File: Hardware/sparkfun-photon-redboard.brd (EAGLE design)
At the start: 68.6 x 53.3 mm, 54 parts, among them U1 WM-N-BM-14

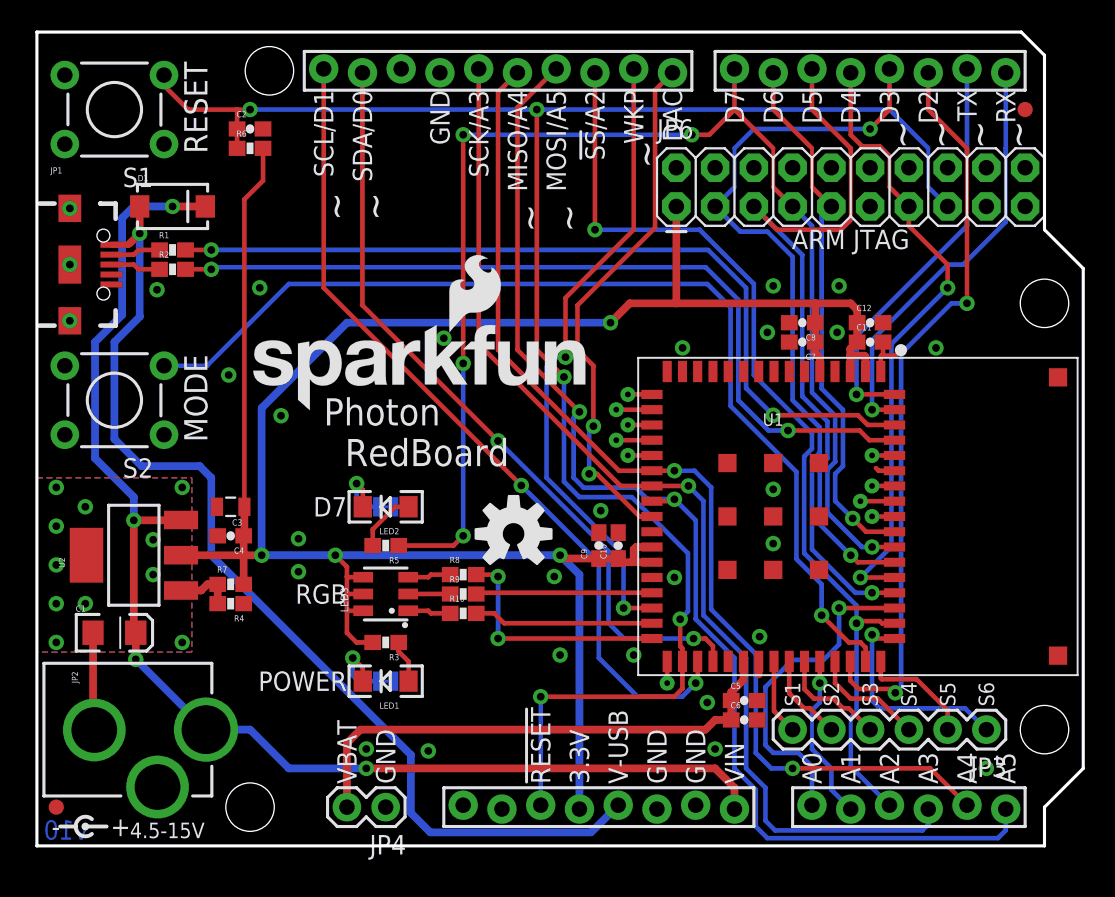
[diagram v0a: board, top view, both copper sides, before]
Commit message: Switched RGB LED and resistor values
-Previous RGB was EOL
-changed resistor values to match existing proven designs (100/100/220)
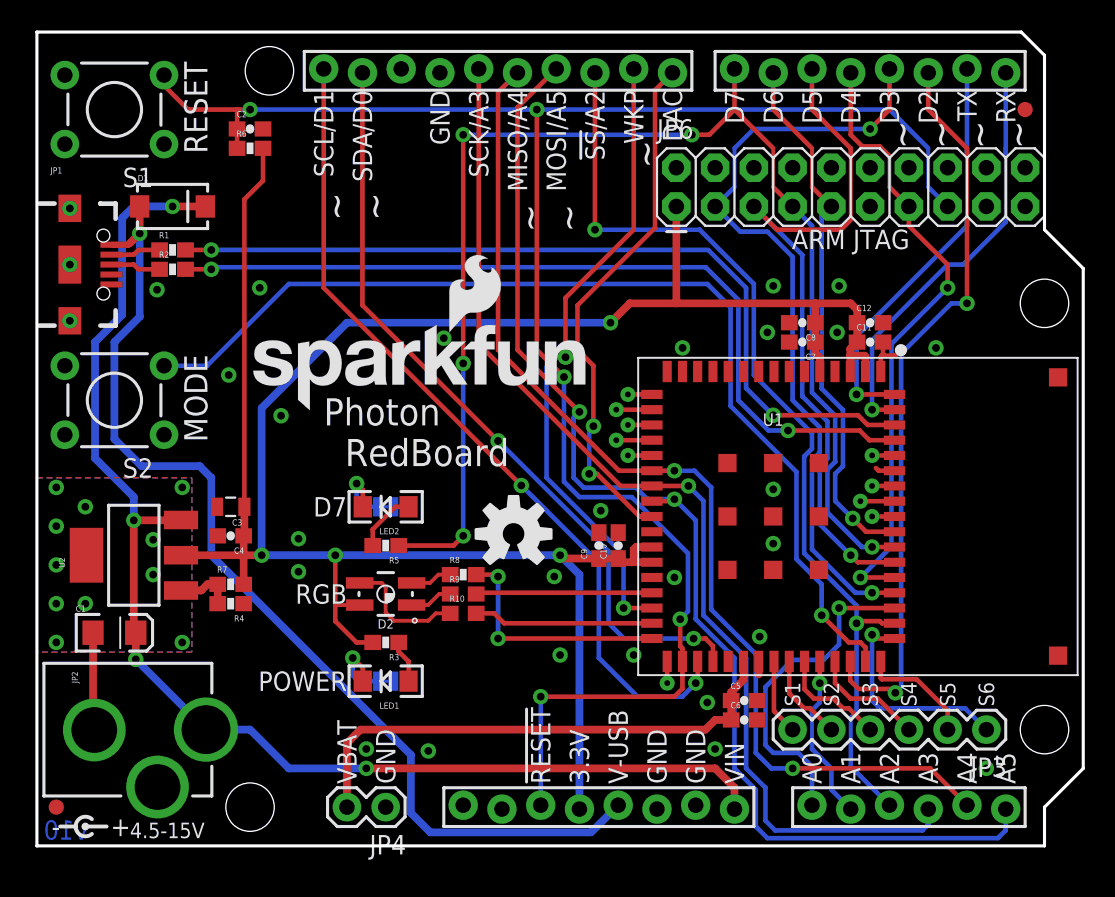
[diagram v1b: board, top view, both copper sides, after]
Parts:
- removed LED3: RGB LED, SparkFun-LED:PLCC-6-LED
- added D2: RGB, SparkFun-LED:P-LCC-4-3
- R10: value 300 -> 100; device SparkFun-Resistors:0603-RES -> SparkFun-Resistors:0603
- R9: value 100 -> 220; device SparkFun-Resistors:0603-RES -> SparkFun-Resistors:0603
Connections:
- removed net N$5: LED3.CB, R10.1
- new net N$9: D2.3, R10.1
- net 3.3V: now also D2.4; no longer LED3.AB, LED3.AG, LED3.AR
- net N$3: now also D2.2; no longer LED3.CG
- net N$4: now also D2.1; no longer LED3.CR
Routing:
- net N$9: track 0.00 -> 8.14 mm
- net N$5: track 2.83 -> 0.00 mm
- net 3.3V: track 158.9 -> 157.3 mm

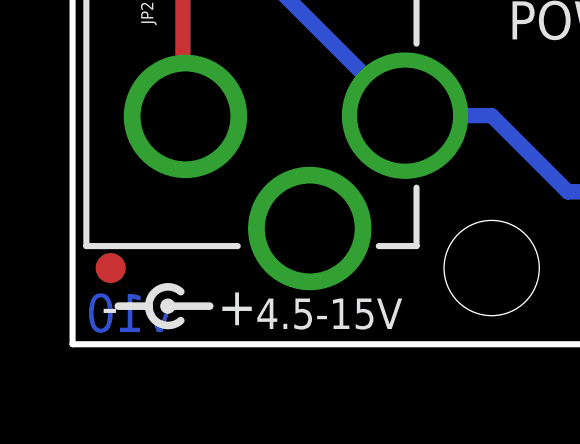
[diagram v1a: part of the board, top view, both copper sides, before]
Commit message: updated version to "v11" in bottom copper and sch
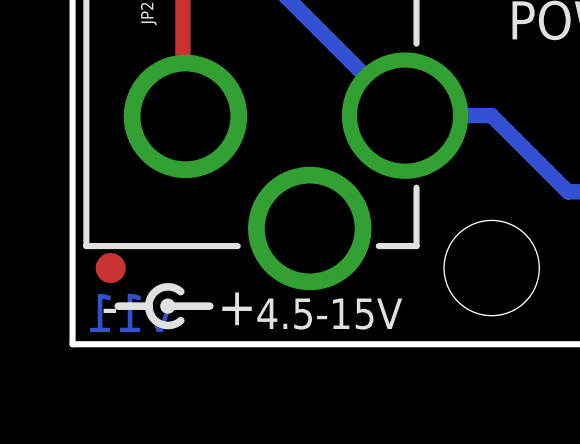
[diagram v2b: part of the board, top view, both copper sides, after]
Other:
- board text added: "v11"
- board text removed: "v10"
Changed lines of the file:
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@@
 <setting verticaltext="up"/>
 </settings>
-<grid distance="0.05" unitdist="inch" unit="inch" style="lines" multiple="1" display="yes" altdistance="0.001" altunitdist="inch" altunit="inch"/>
+<grid distance="0.05" unitdist="inch" unit="inch" style="lines" multiple="1" display="yes" altdistance="0.005" altunitdist="inch" altunit="inch"/>
 <layers>
 <layer number="1" name="Top" color="4" fill="1" visible="yes" active="yes"/>
@@
 <text x="20.32" y="4.064" size="1.27" layer="21" font="vector" ratio="15" rot="R90" align="center-left">VBAT</text>
 <text x="22.86" y="4.064" size="1.27" layer="21" font="vector" ratio="15" rot="R90" align="center-left">GND</text>
-<text x="1.905" y="1.6764" size="1.27" layer="16" font="vector" ratio="15" rot="MR0" align="top-center">v10</text>
+<text x="1.905" y="1.6764" size="1.27" layer="16" font="vector" ratio="15" rot="MR0" align="top-center">v11</text>
 <text x="6.096" y="1.016" size="1.016" layer="21" font="vector" ratio="15" align="center-left">4.5-15V</text>
 <wire x1="1.524" y1="1.27" x2="2.54" y2="1.27" width="0.254" layer="21"/>

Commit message: panelized v11 for production
-note, I also fixed the testpoint so it is exposed on the bottom side (correctly).
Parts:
- flipped TP9 to the top
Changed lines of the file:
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@@
 <layer number="28" name="bValues" color="7" fill="1" visible="no" active="yes"/>
 <layer number="29" name="tStop" color="7" fill="3" visible="no" active="yes"/>
-<layer number="30" name="bStop" color="7" fill="6" visible="no" active="yes"/>
+<layer number="30" name="bStop" color="7" fill="6" visible="yes" active="yes"/>
 <layer number="31" name="tCream" color="7" fill="4" visible="no" active="yes"/>
 <layer number="32" name="bCream" color="7" fill="5" visible="no" active="yes"/>
@@
 <element name="TP7" library="SparkFun-Passives" package="TP_15TH" value="TEST-POINTTP_15TH_THRU" x="37.973" y="26.59" smashed="yes"/>
 <element name="TP8" library="SparkFun-Passives" package="TP_15TH" value="TEST-POINTTP_15TH_THRU" x="38.735" y="25.59" smashed="yes"/>
-<element name="TP9" library="SparkFun-Passives" package="TP_15TH" value="TEST-POINTTP_15TH_THRU" x="54.737" y="25.59" smashed="yes" rot="MR0"/>
+<element name="TP9" library="SparkFun-Passives" package="TP_15TH" value="TEST-POINTTP_15TH_THRU" x="54.737" y="25.59" smashed="yes"/>
 <element name="TP10" library="SparkFun-Passives" package="TP_15TH" value="TEST-POINTTP_15TH_THRU" x="41.31" y="10.668" smashed="yes"/>
 <element name="SJ1" library="SparkFun-Passives" package="PAD-JUMPER-2-NC_BY_TRACE_YES_SILK" value="PWR-LED" x="22.86" y="10.795" smashed="yes" rot="MR0">
